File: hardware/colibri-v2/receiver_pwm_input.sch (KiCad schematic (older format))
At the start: 17 parts

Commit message: Annotated Components
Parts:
- gave numbers to parts that had none: 13
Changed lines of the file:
@@
 P 4750 1550
 AR Path="/5618EF39/56197697" Ref="U?"  Part="1"
-AR Path="/56196EB9/56197697" Ref="U?"  Part="1"
-F 0 "U?" H 4800 1750 60  0000 C CNN
+AR Path="/56196EB9/56197697" Ref="U21"  Part="1"
+F 0 "U21" H 4800 1750 60  0000 C CNN
 F 1 "SN74LVC07APW" H 4800 1250 60  0000 C CNN
 F 2 "" H 4750 1550 60  0000 C CNN
@@
 $EndComp
 $Comp
-L CONN_01X03 P?
+L CONN_01X03 P18
 U 1 1 5619769E
 P 6700 1650
-F 0 "P?" H 6700 1850 50  0000 C CNN
+F 0 "P18" H 6700 1850 50  0000 C CNN
 F 1 "CONN_01X03" V 6800 1650 50  0000 C CNN
 F 2 "" H 6700 1650 60  0000 C CNN
@@
 $EndComp
 $Comp
-L +5V #PWR?
+L +5V #PWR186
 U 1 1 561976A5
 P 6350 1450
-F 0 "#PWR?" H 6350 1300 50  0001 C CNN
+F 0 "#PWR186" H 6350 1300 50  0001 C CNN
 F 1 "+5V" H 6350 1590 50  0000 C CNN
 F 2 "" H 6350 1450 60  0000 C CNN
@@
 $EndComp
 $Comp
-L GND #PWR?
+L GND #PWR187
 U 1 1 561976AB
 P 6350 1850
-F 0 "#PWR?" H 6350 1600 50  0001 C CNN
+F 0 "#PWR187" H 6350 1600 50  0001 C CNN
 F 1 "GND" H 6350 1700 50  0000 C CNN
 F 2 "" H 6350 1850 60  0000 C CNN
@@
 $EndComp
 $Comp
-L R R?
+L R R133
 U 1 1 561976B1
 P 5950 1550
-F 0 "R?" V 6030 1550 50  0000 C CNN
+F 0 "R133" V 6030 1550 50  0000 C CNN
 F 1 "100" V 5950 1550 50  0000 C CNN
 F 2 "" V 5880 1550 30  0000 C CNN
@@
 P 4750 2550
 AR Path="/5618EF39/56197788" Ref="U?"  Part="1"
-AR Path="/56196EB9/56197788" Ref="U?"  Part="2"
-F 0 "U?" H 4800 2750 60  0000 C CNN
+AR Path="/56196EB9/56197788" Ref="U21"  Part="2"
+F 0 "U21" H 4800 2750 60  0000 C CNN
 F 1 "SN74LVC07APW" H 4800 2250 60  0000 C CNN
 F 2 "" H 4750 2550 60  0000 C CNN
@@
 $EndComp
 $Comp
-L CONN_01X03 P?
+L CONN_01X03 P19
 U 1 1 5619778E
 P 6700 2650
-F 0 "P?" H 6700 2850 50  0000 C CNN
+F 0 "P19" H 6700 2850 50  0000 C CNN
 F 1 "CONN_01X03" V 6800 2650 50  0000 C CNN
 F 2 "" H 6700 2650 60  0000 C CNN
@@
 $EndComp
 $Comp
-L +5V #PWR?
+L +5V #PWR188
 U 1 1 56197794
 P 6350 2450
-F 0 "#PWR?" H 6350 2300 50  0001 C CNN
+F 0 "#PWR188" H 6350 2300 50  0001 C CNN
 F 1 "+5V" H 6350 2590 50  0000 C CNN
 F 2 "" H 6350 2450 60  0000 C CNN
@@
 $EndComp
 $Comp
-L GND #PWR?
+L GND #PWR189
 U 1 1 5619779A
 P 6350 2850
-F 0 "#PWR?" H 6350 2600 50  0001 C CNN
+F 0 "#PWR189" H 6350 2600 50  0001 C CNN
 F 1 "GND" H 6350 2700 50  0000 C CNN
 F 2 "" H 6350 2850 60  0000 C CNN
@@
 $EndComp
 $Comp
-L R R?
+L R R134
 U 1 1 561977A0
 P 5950 2550
-F 0 "R?" V 6030 2550 50  0000 C CNN
+F 0 "R134" V 6030 2550 50  0000 C CNN
 F 1 "100" V 5950 2550 50  0000 C CNN
 F 2 "" V 5880 2550 30  0000 C CNN
@@
 P 4750 3550
 AR Path="/5618EF39/561979AC" Ref="U?"  Part="1"
-AR Path="/56196EB9/561979AC" Ref="U?"  Part="3"
-F 0 "U?" H 4800 3750 60  0000 C CNN
+AR Path="/56196EB9/561979AC" Ref="U21"  Part="3"
+F 0 "U21" H 4800 3750 60  0000 C CNN
 F 1 "SN74LVC07APW" H 4800 3250 60  0000 C CNN
 F 2 "" H 4750 3550 60  0000 C CNN
@@
 $EndComp
 $Comp
-L CONN_01X03 P?
+L CONN_01X03 P20
 U 1 1 561979B2
 P 6700 3650
-F 0 "P?" H 6700 3850 50  0000 C CNN
+F 0 "P20" H 6700 3850 50  0000 C CNN
 F 1 "CONN_01X03" V 6800 3650 50  0000 C CNN
 F 2 "" H 6700 3650 60  0000 C CNN
@@
 $EndComp
 $Comp
-L +5V #PWR?
+L +5V #PWR190
 U 1 1 561979B8
 P 6350 3450
-F 0 "#PWR?" H 6350 3300 50  0001 C CNN
+F 0 "#PWR190" H 6350 3300 50  0001 C CNN
 F 1 "+5V" H 6350 3590 50  0000 C CNN
 F 2 "" H 6350 3450 60  0000 C CNN
@@
 $EndComp
 $Comp
-L GND #PWR?
+L GND #PWR191
 U 1 1 561979BE
 P 6350 3850
-F 0 "#PWR?" H 6350 3600 50  0001 C CNN
+F 0 "#PWR191" H 6350 3600 50  0001 C CNN
 F 1 "GND" H 6350 3700 50  0000 C CNN
 F 2 "" H 6350 3850 60  0000 C CNN
@@
 $EndComp
 $Comp
-L R R?
+L R R135
 U 1 1 561979C4
 P 5950 3550
-F 0 "R?" V 6030 3550 50  0000 C CNN
+F 0 "R135" V 6030 3550 50  0000 C CNN
 F 1 "100" V 5950 3550 50  0000 C CNN
 F 2 "" V 5880 3550 30  0000 C CNN
@@
 P 4750 4550
 AR Path="/5618EF39/561979D2" Ref="U?"  Part="1"
-AR Path="/56196EB9/561979D2" Ref="U?"  Part="4"
-F 0 "U?" H 4800 4750 60  0000 C CNN
+AR Path="/56196EB9/561979D2" Ref="U21"  Part="4"
+F 0 "U21" H 4800 4750 60  0000 C CNN
 F 1 "SN74LVC07APW" H 4800 4250 60  0000 C CNN
 F 2 "" H 4750 4550 60  0000 C CNN
@@
 $EndComp
 $Comp
-L CONN_01X03 P?
+L CONN_01X03 P21
 U 1 1 561979D8
 P 6700 4650
-F 0 "P?" H 6700 4850 50  0000 C CNN
+F 0 "P21" H 6700 4850 50  0000 C CNN
 F 1 "CONN_01X03" V 6800 4650 50  0000 C CNN
 F 2 "" H 6700 4650 60  0000 C CNN
@@
 $EndComp
 $Comp
-L +5V #PWR?
+L +5V #PWR192
 U 1 1 561979DE
 P 6350 4450
-F 0 "#PWR?" H 6350 4300 50  0001 C CNN
+F 0 "#PWR192" H 6350 4300 50  0001 C CNN
 F 1 "+5V" H 6350 4590 50  0000 C CNN
 F 2 "" H 6350 4450 60  0000 C CNN
@@
 $EndComp
 $Comp
-L GND #PWR?
+L GND #PWR193
 U 1 1 561979E4
 P 6350 4850
-F 0 "#PWR?" H 6350 4600 50  0001 C CNN
+F 0 "#PWR193" H 6350 4600 50  0001 C CNN
 F 1 "GND" H 6350 4700 50  0000 C CNN
 F 2 "" H 6350 4850 60  0000 C CNN
@@
 $EndComp
 $Comp
-L R R?
+L R R136
 U 1 1 561979EA
 P 5950 4550
-F 0 "R?" V 6030 4550 50  0000 C CNN
+F 0 "R136" V 6030 4550 50  0000 C CNN
 F 1 "100" V 5950 4550 50  0000 C CNN
 F 2 "" V 5880 4550 30  0000 C CNN
@@
 	3800 4550 4300 4550
 $Comp
-L SN74LVC07APW U?
+L SN74LVC07APW U21
 U 7 1 56198271
 P 4750 6550
-F 0 "U?" H 4800 6750 60  0000 C CNN
+F 0 "U21" H 4800 6750 60  0000 C CNN
 F 1 "SN74LVC07APW" H 4800 6250 60  0000 C CNN
 F 2 "" H 4750 6550 60  0000 C CNN
@@
 $EndComp
 $Comp
-L GND #PWR?
+L GND #PWR184
 U 1 1 56198278
 P 5400 6850
-F 0 "#PWR?" H 5400 6600 50  0001 C CNN
+F 0 "#PWR184" H 5400 6600 50  0001 C CNN
 F 1 "GND" H 5400 6700 50  0000 C CNN
 F 2 "" H 5400 6850 60  0000 C CNN
@@
 	5400 6650 5400 6850
 $Comp
-L +3V3 #PWR?
+L +3V3 #PWR183
 U 1 1 56198280
 P 5400 6300
-F 0 "#PWR?" H 5400 6150 50  0001 C CNN
+F 0 "#PWR183" H 5400 6150 50  0001 C CNN
 F 1 "+3V3" H 5400 6440 50  0000 C CNN
 F 2 "" H 5400 6300 60  0000 C CNN
@@
 	5600 6450 5200 6450
 $Comp
-L GND #PWR?
+L GND #PWR185
 U 1 1 56198288
 P 6150 6450
-F 0 "#PWR?" H 6150 6200 50  0001 C CNN
+F 0 "#PWR185" H 6150 6200 50  0001 C CNN
 F 1 "GND" H 6150 6300 50  0000 C CNN
 F 2 "" H 6150 6450 60  0000 C CNN
@@
 	5900 6450 6150 6450
 $Comp
-L C C?
+L C C92
 U 1 1 56198290
 P 5750 6450
-F 0 "C?" V 5700 6500 50  0000 L CNN
+F 0 "C92" V 5700 6500 50  0000 L CNN
 F 1 "100n/50V" V 5900 6250 50  0000 L CNN
 F 2 "" H 5788 6300 30  0000 C CNN
@@
 P 4750 5550
 AR Path="/5618EF39/5619865A" Ref="U?"  Part="1"
-AR Path="/56196EB9/5619865A" Ref="U?"  Part="5"
-F 0 "U?" H 4800 5750 60  0000 C CNN
+AR Path="/56196EB9/5619865A" Ref="U19"  Part="5"
+F 0 "U19" H 4800 5750 60  0000 C CNN
 F 1 "SN74LVC07APW" H 4800 5250 60  0000 C CNN
 F 2 "" H 4750 5550 60  0000 C CNN
@@
 $EndComp
 $Comp
-L CONN_01X03 P?
+L CONN_01X03 P22
 U 1 1 56198660
 P 6700 5650
-F 0 "P?" H 6700 5850 50  0000 C CNN
+F 0 "P22" H 6700 5850 50  0000 C CNN
 F 1 "CONN_01X03" V 6800 5650 50  0000 C CNN
 F 2 "" H 6700 5650 60  0000 C CNN
@@
 $EndComp
 $Comp
-L +5V #PWR?
+L +5V #PWR194
 U 1 1 56198666
 P 6350 5450
-F 0 "#PWR?" H 6350 5300 50  0001 C CNN
+F 0 "#PWR194" H 6350 5300 50  0001 C CNN
 F 1 "+5V" H 6350 5590 50  0000 C CNN
 F 2 "" H 6350 5450 60  0000 C CNN
@@
 $EndComp
 $Comp
-L GND #PWR?
+L GND #PWR195
 U 1 1 5619866C
 P 6350 5850
-F 0 "#PWR?" H 6350 5600 50  0001 C CNN
+F 0 "#PWR195" H 6350 5600 50  0001 C CNN
 F 1 "GND" H 6350 5700 50  0000 C CNN
 F 2 "" H 6350 5850 60  0000 C CNN
@@
 $EndComp
 $Comp
-L R R?
+L R R137
 U 1 1 56198672
 P 5950 5550
-F 0 "R?" V 6030 5550 50  0000 C CNN
+F 0 "R137" V 6030 5550 50  0000 C CNN
 F 1 "100" V 5950 5550 50  0000 C CNN
 F 2 "" V 5880 5550 30  0000 C CNN

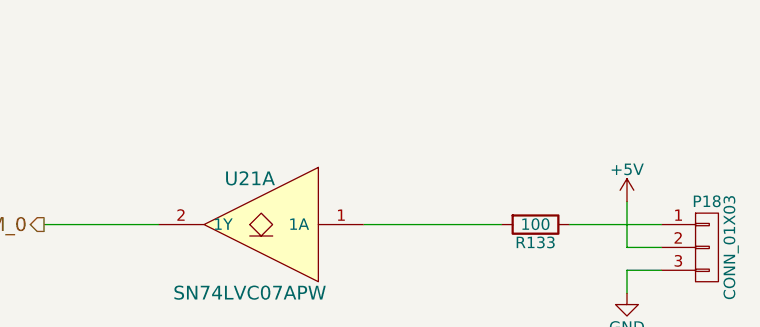
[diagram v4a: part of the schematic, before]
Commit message: Reworked the buttons/leds sheet
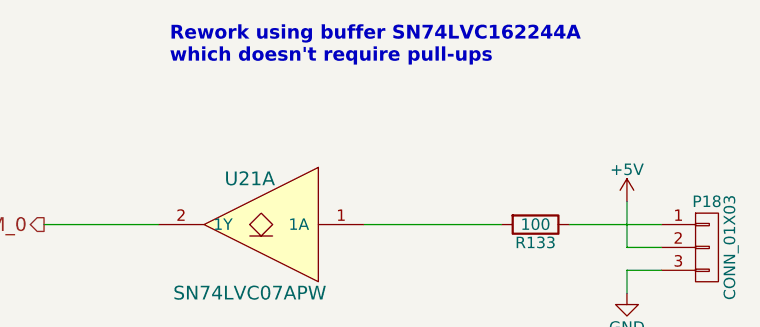
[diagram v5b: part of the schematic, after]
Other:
- note added: "Rework using buffer SN74LVC162244A\nwhich doesn't require pull-ups"
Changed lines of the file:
@@
 Wire Wire Line
 	3800 5550 4300 5550
+Text Notes 4350 850  0    60   ~ 12
+Rework using buffer SN74LVC162244A\nwhich doesn't require pull-ups
 $EndSCHEMATC

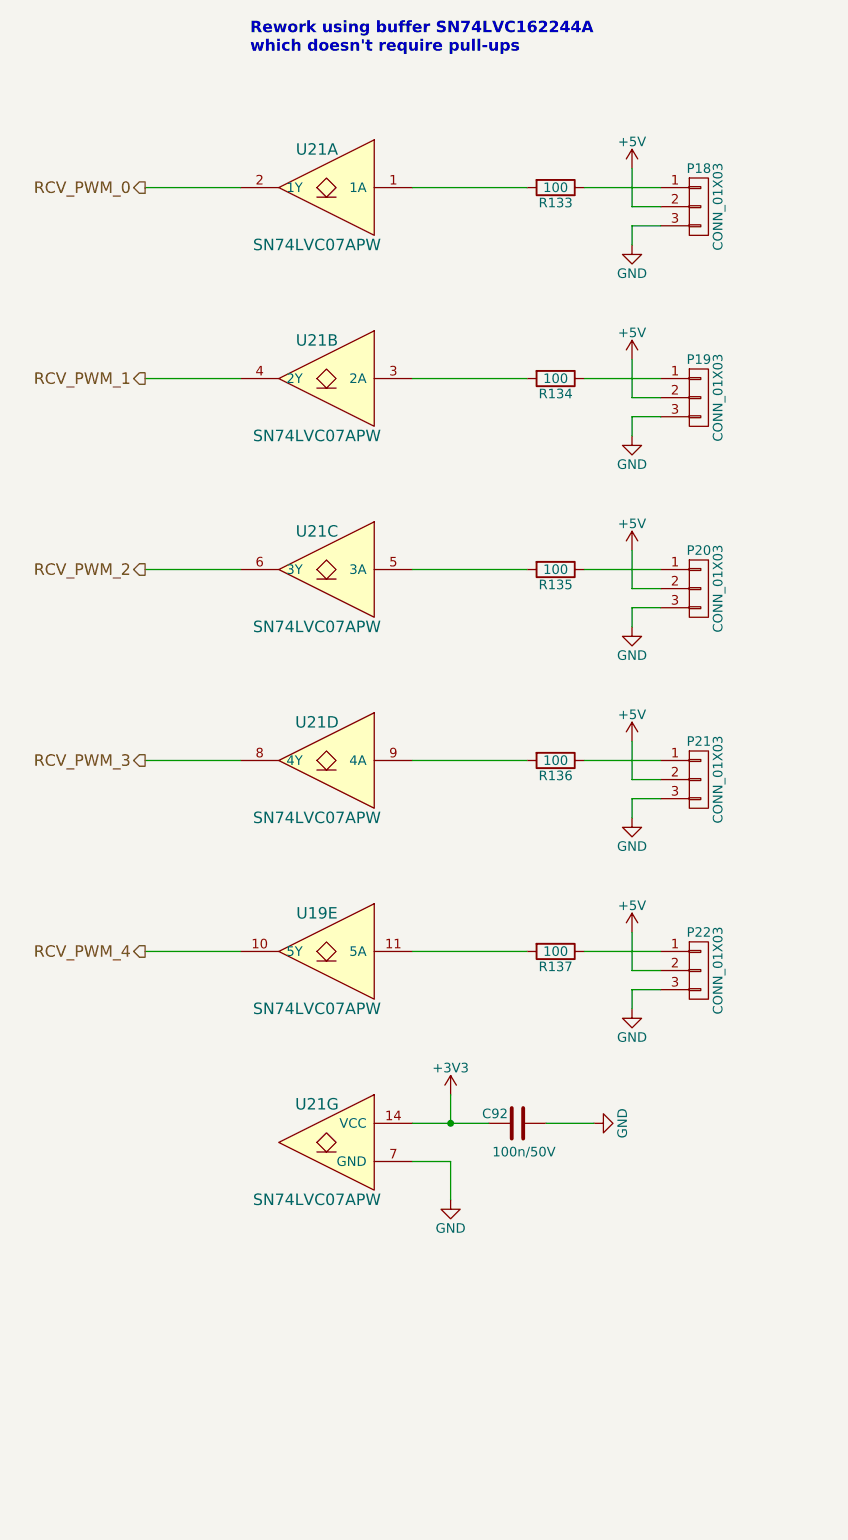
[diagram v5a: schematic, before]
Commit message: Replaced PWM buffers with SN74LVC162244A, which doesn't require pull-ups
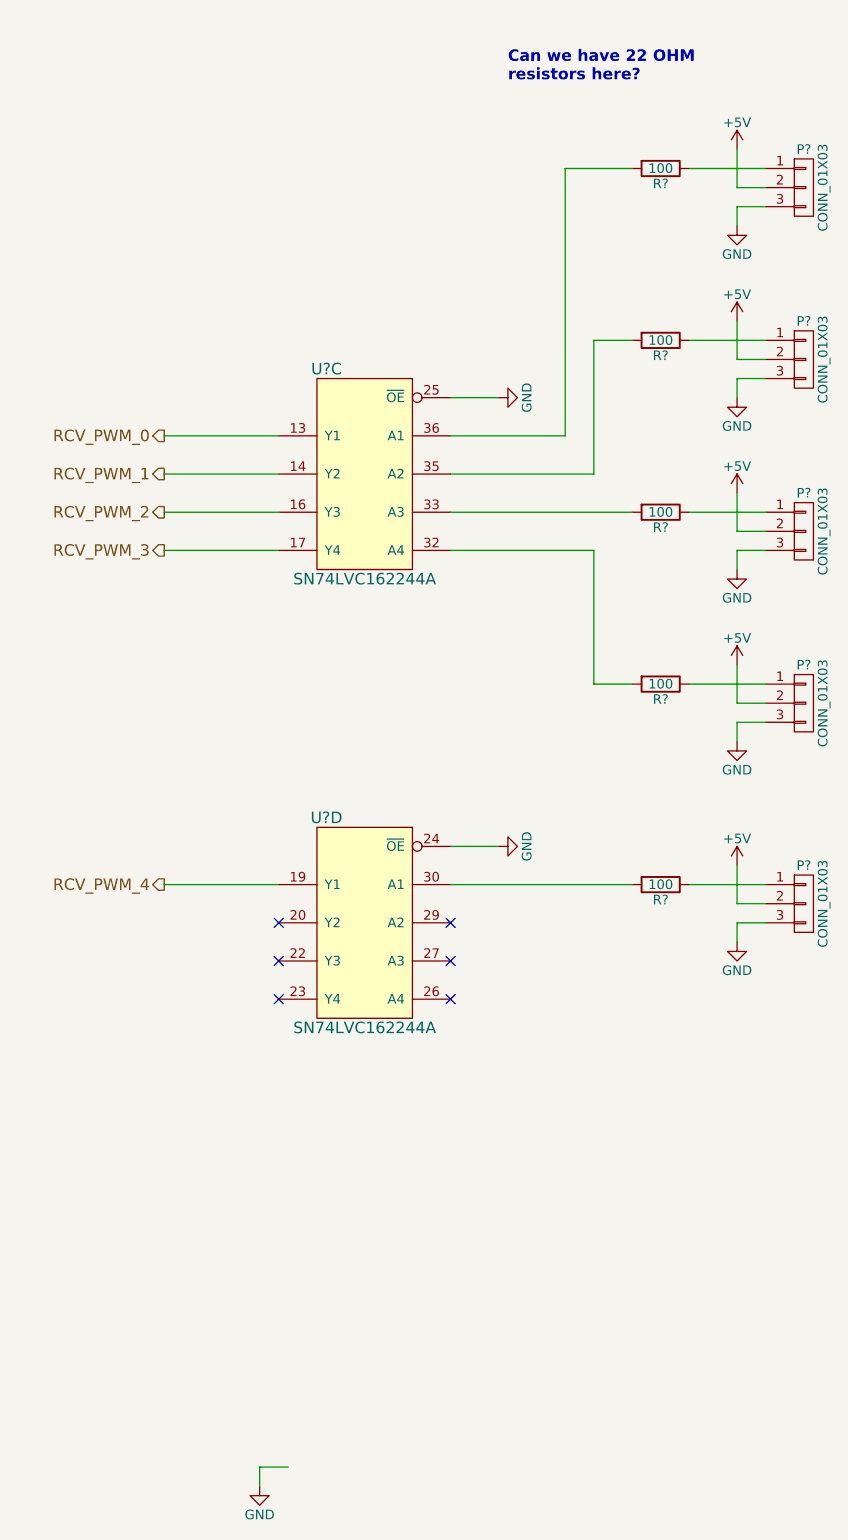
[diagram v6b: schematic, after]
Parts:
- removed C92: 100n/50V, symbol C
- removed P18, P19, P20, P21, P22: CONN_01X03, symbol CONN_01X03
- removed R133, R134, R135, R136, R137: 100, symbol R
- removed U19, U21: SN74LVC07APW, symbol SN74LVC07APW
- added P? (x5): CONN_01X03, symbol CONN_01X03
- added R? (x5): 100, symbol R
- added U? (x2): SN74LVC162244A, symbol SN74LVC162244A
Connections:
- net +5V: now also P?.2 (P2), P?.2 (P2), P?.2 (P2), P?.2 (P2), P?.2 (P2)
- net GND: now also P?.3 (P3), P?.3 (P3), P?.3 (P3), P?.3 (P3), P?.3 (P3), U?.24 (~OE), U?.25 (~OE)
- net RCV_PWM_0: now also U?.13 (Y1)
- net RCV_PWM_1: now also U?.14 (Y2)
- net RCV_PWM_2: now also U?.16 (Y3)
- net RCV_PWM_3: now also U?.17 (Y4)
- net RCV_PWM_4: now also U?.19 (Y1)
- new net: P?.1 (P1), R?.1 (x5)
- new net: R?.2, U?.36 (A1)
- new net: R?.2, U?.35 (A2)
- new net: R?.2, U?.33 (A3)
- new net: R?.2, U?.32 (A4)
- new net: R?.2, U?.30 (A1)
- no-connect marks 0 -> 6
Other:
- note added: "Can we have 22 OHM \nresistors here?"
- note removed: "Rework using buffer SN74LVC162244A\nwhich doesn't require pull-ups"

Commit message: Re-annotated schematic
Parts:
- gave numbers to parts that had none: 11
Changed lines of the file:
@@
 Can we have 22 OHM \nresistors here?
 $Comp
-L CONN_01X03 P?
+L CONN_01X03 P18
 U 1 1 5624B1D9
 P 7250 1550
-F 0 "P?" H 7250 1750 50  0000 C CNN
+F 0 "P18" H 7250 1750 50  0000 C CNN
 F 1 "CONN_01X03" V 7350 1550 50  0000 C CNN
 F 2 "" H 7250 1550 60  0000 C CNN
@@
 $EndComp
 $Comp
-L +5V #PWR?
+L +5V #PWR183
 U 1 1 5624B1E0
 P 6900 1350
-F 0 "#PWR?" H 6900 1200 50  0001 C CNN
+F 0 "#PWR183" H 6900 1200 50  0001 C CNN
 F 1 "+5V" H 6900 1490 50  0000 C CNN
 F 2 "" H 6900 1350 60  0000 C CNN
@@
 $EndComp
 $Comp
-L GND #PWR?
+L GND #PWR184
 U 1 1 5624B1E6
 P 6900 1750
-F 0 "#PWR?" H 6900 1500 50  0001 C CNN
+F 0 "#PWR184" H 6900 1500 50  0001 C CNN
 F 1 "GND" H 6900 1600 50  0000 C CNN
 F 2 "" H 6900 1750 60  0000 C CNN
@@
 $EndComp
 $Comp
-L R R?
+L R R136
 U 1 1 5624B1EC
 P 6500 1450
-F 0 "R?" V 6580 1450 50  0000 C CNN
+F 0 "R136" V 6580 1450 50  0000 C CNN
 F 1 "100" V 6500 1450 50  0000 C CNN
 F 2 "" V 6430 1450 30  0000 C CNN
@@
 $EndComp
 $Comp
-L CONN_01X03 P?
+L CONN_01X03 P19
 U 1 1 5624B1F9
 P 7250 2450
-F 0 "P?" H 7250 2650 50  0000 C CNN
+F 0 "P19" H 7250 2650 50  0000 C CNN
 F 1 "CONN_01X03" V 7350 2450 50  0000 C CNN
 F 2 "" H 7250 2450 60  0000 C CNN
@@
 $EndComp
 $Comp
-L +5V #PWR?
+L +5V #PWR185
 U 1 1 5624B200
 P 6900 2250
-F 0 "#PWR?" H 6900 2100 50  0001 C CNN
+F 0 "#PWR185" H 6900 2100 50  0001 C CNN
 F 1 "+5V" H 6900 2390 50  0000 C CNN
 F 2 "" H 6900 2250 60  0000 C CNN
@@
 $EndComp
 $Comp
-L GND #PWR?
+L GND #PWR186
 U 1 1 5624B206
 P 6900 2650
-F 0 "#PWR?" H 6900 2400 50  0001 C CNN
+F 0 "#PWR186" H 6900 2400 50  0001 C CNN
 F 1 "GND" H 6900 2500 50  0000 C CNN
 F 2 "" H 6900 2650 60  0000 C CNN
@@
 $EndComp
 $Comp
-L R R?
+L R R137
 U 1 1 5624B20C
 P 6500 2350
-F 0 "R?" V 6580 2350 50  0000 C CNN
+F 0 "R137" V 6580 2350 50  0000 C CNN
 F 1 "100" V 6500 2350 50  0000 C CNN
 F 2 "" V 6430 2350 30  0000 C CNN
@@
 $EndComp
 $Comp
-L CONN_01X03 P?
+L CONN_01X03 P20
 U 1 1 5624B219
 P 7250 3350
-F 0 "P?" H 7250 3550 50  0000 C CNN
+F 0 "P20" H 7250 3550 50  0000 C CNN
 F 1 "CONN_01X03" V 7350 3350 50  0000 C CNN
 F 2 "" H 7250 3350 60  0000 C CNN
@@
 $EndComp
 $Comp
-L +5V #PWR?
+L +5V #PWR187
 U 1 1 5624B220
 P 6900 3150
-F 0 "#PWR?" H 6900 3000 50  0001 C CNN
+F 0 "#PWR187" H 6900 3000 50  0001 C CNN
 F 1 "+5V" H 6900 3290 50  0000 C CNN
 F 2 "" H 6900 3150 60  0000 C CNN
@@
 $EndComp
 $Comp
-L GND #PWR?
+L GND #PWR188
 U 1 1 5624B226
 P 6900 3550
-F 0 "#PWR?" H 6900 3300 50  0001 C CNN
+F 0 "#PWR188" H 6900 3300 50  0001 C CNN
 F 1 "GND" H 6900 3400 50  0000 C CNN
 F 2 "" H 6900 3550 60  0000 C CNN
@@
 $EndComp
 $Comp
-L R R?
+L R R138
 U 1 1 5624B22C
 P 6500 3250
-F 0 "R?" V 6580 3250 50  0000 C CNN
+F 0 "R138" V 6580 3250 50  0000 C CNN
 F 1 "100" V 6500 3250 50  0000 C CNN
 F 2 "" V 6430 3250 30  0000 C CNN
@@
 $EndComp
 $Comp
-L CONN_01X03 P?
+L CONN_01X03 P21
 U 1 1 5624B239
 P 7250 4250
-F 0 "P?" H 7250 4450 50  0000 C CNN
+F 0 "P21" H 7250 4450 50  0000 C CNN
 F 1 "CONN_01X03" V 7350 4250 50  0000 C CNN
 F 2 "" H 7250 4250 60  0000 C CNN
@@
 $EndComp
 $Comp
-L +5V #PWR?
+L +5V #PWR189
 U 1 1 5624B240
 P 6900 4050
-F 0 "#PWR?" H 6900 3900 50  0001 C CNN
+F 0 "#PWR189" H 6900 3900 50  0001 C CNN
 F 1 "+5V" H 6900 4190 50  0000 C CNN
 F 2 "" H 6900 4050 60  0000 C CNN
@@
 $EndComp
 $Comp
-L GND #PWR?
+L GND #PWR190
 U 1 1 5624B246
 P 6900 4450
-F 0 "#PWR?" H 6900 4200 50  0001 C CNN
+F 0 "#PWR190" H 6900 4200 50  0001 C CNN
 F 1 "GND" H 6900 4300 50  0000 C CNN
 F 2 "" H 6900 4450 60  0000 C CNN
@@
 $EndComp
 $Comp
-L R R?
+L R R139
 U 1 1 5624B24C
 P 6500 4150
-F 0 "R?" V 6580 4150 50  0000 C CNN
+F 0 "R139" V 6580 4150 50  0000 C CNN
 F 1 "100" V 6500 4150 50  0000 C CNN
 F 2 "" V 6430 4150 30  0000 C CNN
@@
 $EndComp
 $Comp
-L SN74LVC162244A U?
-U 3 1 5624B259
+L SN74LVC162244A U19
+U 4 1 5624B259
 P 4950 3050
-F 0 "U?" H 5150 3600 60  0000 C CNN
+F 0 "U19" H 5150 3600 60  0000 C CNN
 F 1 "SN74LVC162244A" H 4950 2500 60  0000 C CNN
 F 2 "" H 4950 2900 60  0000 C CNN
 F 3 "" H 4950 2900 60  0000 C CNN
-	3    4950 3050
+	4    4950 3050
 	-1   0    0    -1
 $EndComp
@@
 RCV_PWM_4
 $Comp
-L CONN_01X03 P?
+L CONN_01X03 P22
 U 1 1 5624BF56
 P 7250 5300
-F 0 "P?" H 7250 5500 50  0000 C CNN
+F 0 "P22" H 7250 5500 50  0000 C CNN
 F 1 "CONN_01X03" V 7350 5300 50  0000 C CNN
 F 2 "" H 7250 5300 60  0000 C CNN
@@
 $EndComp
 $Comp
-L +5V #PWR?
+L +5V #PWR191
 U 1 1 5624BF5C
 P 6900 5100
-F 0 "#PWR?" H 6900 4950 50  0001 C CNN
+F 0 "#PWR191" H 6900 4950 50  0001 C CNN
 F 1 "+5V" H 6900 5240 50  0000 C CNN
 F 2 "" H 6900 5100 60  0000 C CNN
@@
 $EndComp
 $Comp
-L GND #PWR?
+L GND #PWR192
 U 1 1 5624BF62
 P 6900 5500
-F 0 "#PWR?" H 6900 5250 50  0001 C CNN
+F 0 "#PWR192" H 6900 5250 50  0001 C CNN
 F 1 "GND" H 6900 5350 50  0000 C CNN
 F 2 "" H 6900 5500 60  0000 C CNN
@@
 $EndComp
 $Comp
-L R R?
+L R R140
 U 1 1 5624BF68
 P 6500 5200
-F 0 "R?" V 6580 5200 50  0000 C CNN
+F 0 "R140" V 6580 5200 50  0000 C CNN
 F 1 "100" V 6500 5200 50  0000 C CNN
 F 2 "" V 6430 5200 30  0000 C CNN
@@
 $EndComp
 $Comp
-L GND #PWR?
+L GND #PWR180
 U 1 1 5624BFB9
 P 4400 8350
-F 0 "#PWR?" H 4400 8100 50  0001 C CNN
+F 0 "#PWR180" H 4400 8100 50  0001 C CNN
 F 1 "GND" H 4400 8200 50  0000 C CNN
 F 2 "" H 4400 8350 60  0000 C CNN
@@
 $EndComp
 $Comp
-L SN74LVC162244A U?
-U 4 1 5624BFCA
+L SN74LVC162244A U19
+U 5 1 5624BFCA
 P 4950 5400
-F 0 "U?" H 5150 5950 60  0000 C CNN
+F 0 "U19" H 5150 5950 60  0000 C CNN
 F 1 "SN74LVC162244A" H 4950 4850 60  0000 C CNN
 F 2 "" H 4950 5250 60  0000 C CNN
 F 3 "" H 4950 5250 60  0000 C CNN
-	4    4950 5400
+	5    4950 5400
 	-1   0    0    -1
 $EndComp
 $Comp
-L GND #PWR?
+L GND #PWR182
 U 1 1 5624BFE2
 P 5650 5000
-F 0 "#PWR?" H 5650 4750 50  0001 C CNN
+F 0 "#PWR182" H 5650 4750 50  0001 C CNN
 F 1 "GND" H 5650 4850 50  0000 C CNN
 F 2 "" H 5650 5000 60  0000 C CNN
@@
 	5400 5000 5650 5000
 $Comp
-L GND #PWR?
+L GND #PWR181
 U 1 1 5624F657
 P 5650 2650
-F 0 "#PWR?" H 5650 2400 50  0001 C CNN
+F 0 "#PWR181" H 5650 2400 50  0001 C CNN
 F 1 "GND" H 5650 2500 50  0000 C CNN
 F 2 "" H 5650 2650 60  0000 C CNN
